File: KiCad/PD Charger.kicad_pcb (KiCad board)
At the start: 4 copper layers, 74 x 46 mm, 132 parts, among them J1 USB_C_Receptacle_USB2.0, J2 Conn_ARM_SWD_TagConnect_TC2030, J3 XT60_M, Q1 NMOS, Q2 NMOS, Q3 NMOS, Q4 NMOS, Q5 SiR5607DP, Q6 SiR5607DP, Q7 SiR5607DP, Q8 SiR5607DP, Q9 Q_Dual_NMOS_S1G1D2S2G2D1, SW1 SW_MEC_5G, SW2 SW_MEC_5G, U1 FUSB302B01MPX, U2 LMR36006BRNXT, U3 LT8390xFE, U4 STM32G431CBUx, U5 ADM1270ACPZ, U6 INA293A2, U7 TPD4E05U06DQA

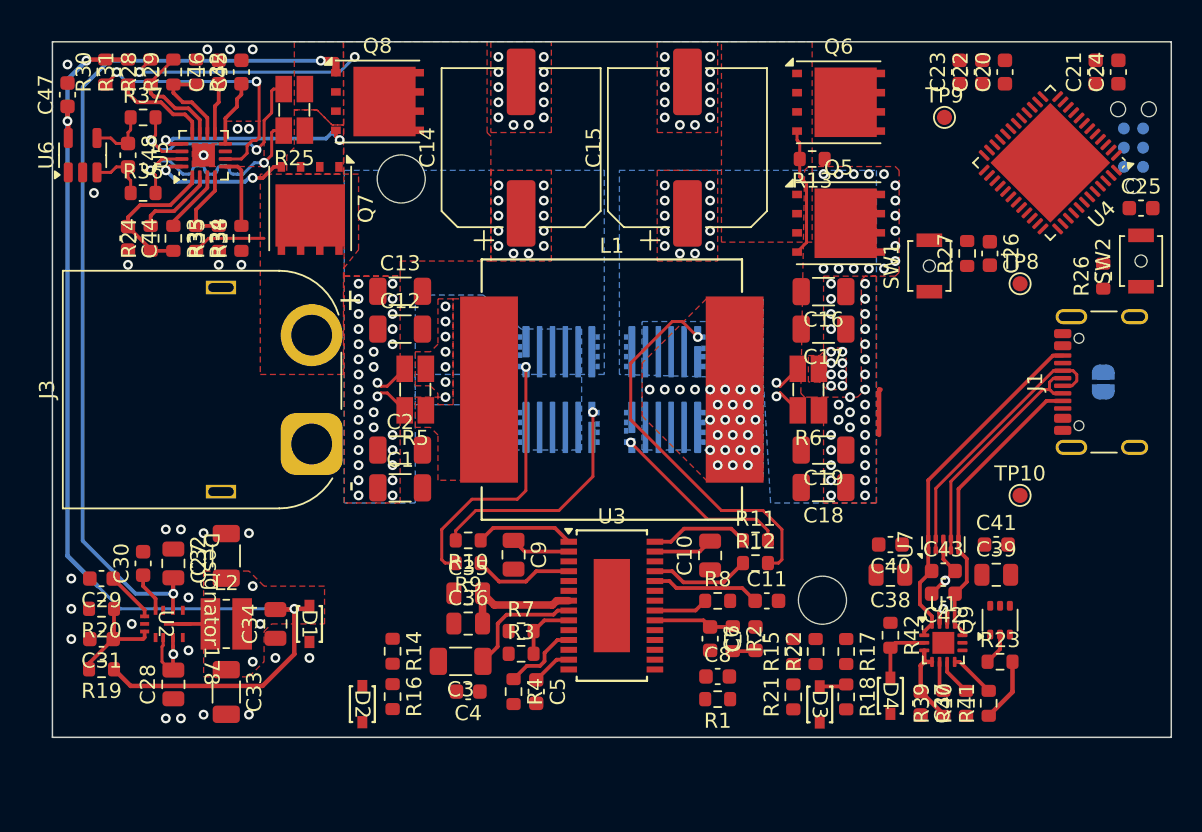
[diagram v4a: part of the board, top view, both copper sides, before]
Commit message: multi sheet redesign
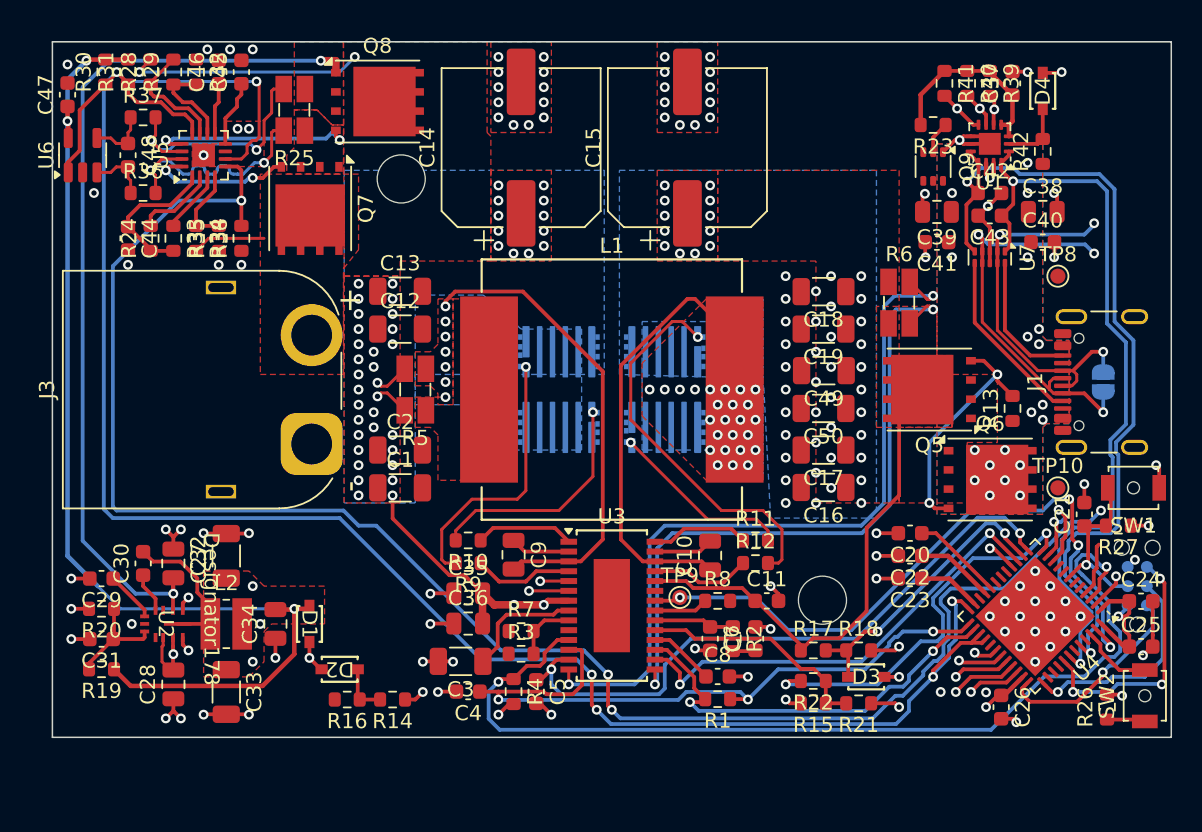
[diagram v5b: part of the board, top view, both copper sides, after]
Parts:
- added C49: 10u, Capacitor_SMD:C_1206_3216Metric, F.Cu at (63.0, 33.8)
- added C50: 10u, Capacitor_SMD:C_1206_3216Metric, F.Cu at (63.0, 36.2)
- moved C37 41.4 mm to (75.5, 14.8), turned to 90 degrees
- moved D4 41.2 mm to (77.5, 15.2), turned to 90 degrees
- moved R39 41.1 mm to (74.0, 14.8), turned to -90 degrees
- moved R41 41.1 mm to (71.0, 14.8), turned to -90 degrees
- moved R40 41.0 mm to (72.5, 14.8), turned to -90 degrees
- moved TP9 36.3 mm to (53.5, 48.8)
- moved R23 35.8 mm to (70.2, 17.5), turned to 180 degrees
- moved C24 35.0 mm to (84.0, 49.0), turned to 0 degrees
- moved C23 33.7 mm to (68.7, 47.5), turned to 180 degrees
- moved R42 33.5 mm to (77.5, 19.2), turned to 90 degrees
- moved U1 33.1 mm to (74.0, 18.8), turned to 180 degrees
- moved C22 32.4 mm to (68.7, 46.0), turned to 180 degrees
- moved C20 31.1 mm to (68.7, 44.5), turned to 180 degrees
- moved Q9 30.3 mm to (70.2, 20.2), turned to -90 degrees
- moved U4 30.0 mm to (77.0, 50.0)
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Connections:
- C4 pad 1: /DC-DC/VREF -> /REG_ON
- R1 pad 1: /DC-DC/VREF -> /REG_ON
- R1 pad 2: /DC-DC/~{PGOOD} -> /~{PGOOD}
- R30 pad 1: /Input Protection/~{FAULT} -> /ISMON
- R31 pad 1: /Input Protection/SGOOD -> /ISMON
- R38 pad 2: /Input Protection/SOURCE_EN -> /SOURCE_EN
- U3 pad 12: /DC-DC/VREF -> /REG_ON
- U3 pad 17: /DC-DC/~{PGOOD} -> /~{PGOOD}
- U4 pad 25: /MCU/REG_ON -> /REG_ON
- U4 pad 26: /MCU/~{PGOOD} -> /~{PGOOD}
- U4 pad 27: /MCU/SGOOD -> /ISMON
- U4 pad 28: /MCU/~{FAULT} -> /ISMON
- U4 pad 4: /MCU/SOURCE_EN -> /SOURCE_EN
- U5 pad 12: /Input Protection/SGOOD -> /ISMON
- U5 pad 5: /Input Protection/SOURCE_EN -> /SOURCE_EN
- U5 pad 6: /Input Protection/~{FAULT} -> /ISMON
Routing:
- net /ISMON: track 0.00 -> 137.3 mm, vias 0 -> 6
- net /SOURCE_EN: track 0.00 -> 115.6 mm, vias 0 -> 4
- net GND: track 4.63 -> 70.2 mm, vias 48 -> 119
- net /LOADEN: track 5.05 -> 65.2 mm, vias 0 -> 2
- net /USB_DN: track 16.1 -> 69.7 mm, vias 0 -> 4
- net /SDA: track 3.04 -> 54.3 mm, vias 0 -> 2
- net /SCL: track 2.43 -> 53.5 mm, vias 0 -> 2
- net /USB_DP: track 18.2 -> 68.7 mm, vias 0 -> 4
- net /~{INT}: track 2.02 -> 51.7 mm, vias 0 -> 2
- net /DC-DC/ISP: track 1.98 -> 50.4 mm, vias 1 -> 2
- net /CC: track 19.8 -> 67.7 mm, vias 0 -> 2
- net /REG_ON: track 0.00 -> 45.7 mm, vias 0 -> 3
- net /SYNC: track 0.00 -> 44.9 mm, vias 0 -> 4
- net /DC-DC/ISN: track 1.98 -> 44.3 mm, vias 1 -> 2
- net /ICTRL: track 2.70 -> 42.7 mm, vias 0 -> 2
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- added copper zone on B.Cu, net VBUS
- added copper zone on F.Cu, net VBUS
- added copper zone on In1.Cu, net VBUS
- added copper zone on In2.Cu, net VBUS
- removed copper zone on In1.Cu, net VD

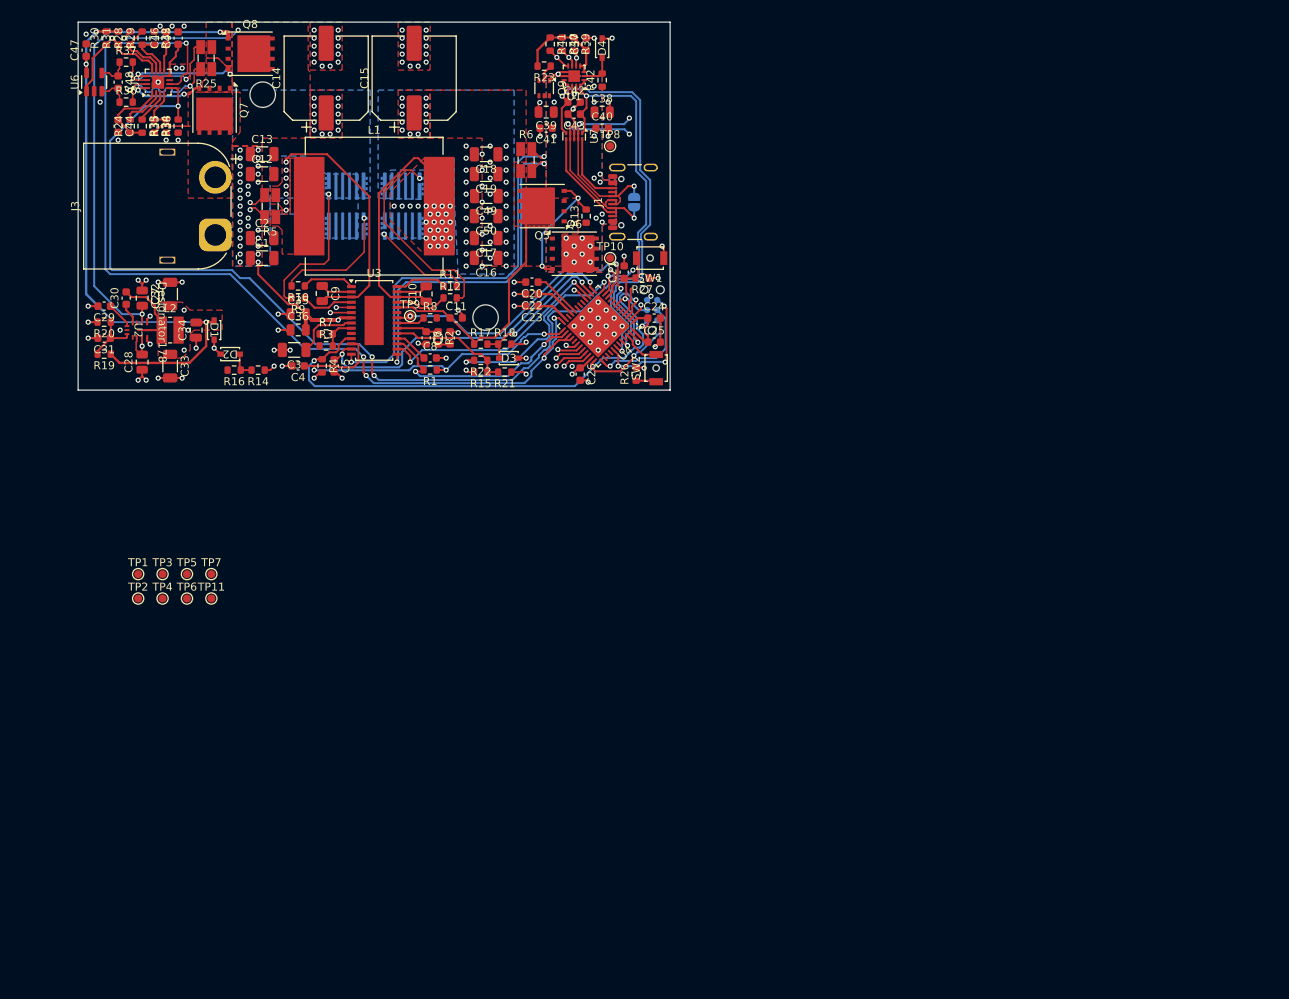
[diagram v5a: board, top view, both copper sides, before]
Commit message: standalone regulator core
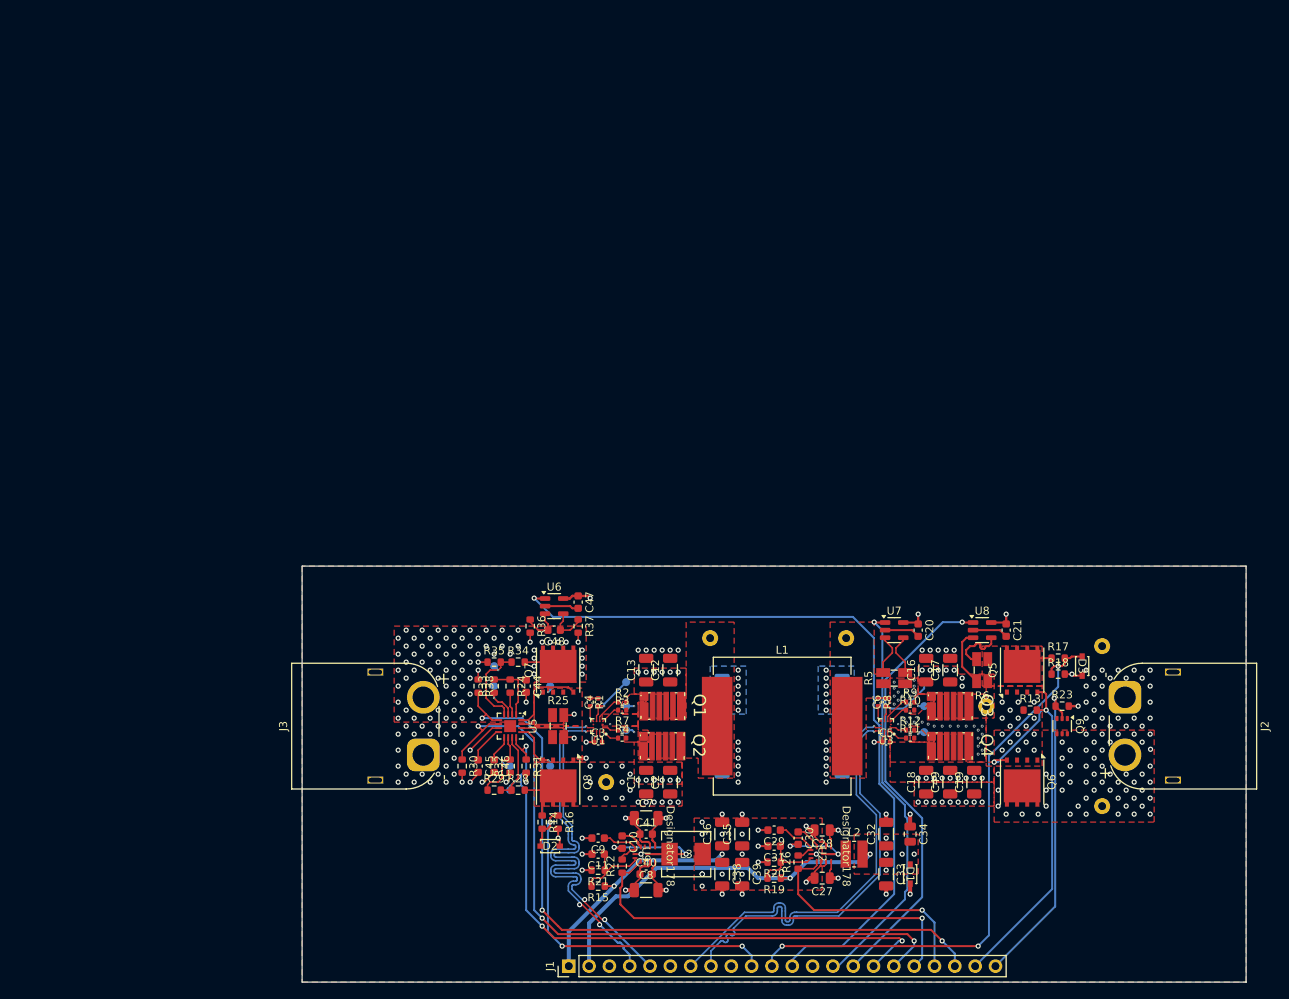
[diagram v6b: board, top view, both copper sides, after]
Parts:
- removed C22, C23, C24, C25: 0.1u, Capacitor_SMD:C_0603_1608Metric
- removed C26: 0.47u, Capacitor_SMD:C_0603_1608Metric
- removed C37: 100n, Capacitor_SMD:C_0603_1608Metric
- removed C42, C43: 330p, Capacitor_SMD:C_0603_1608Metric
- removed C50: 10u, Capacitor_SMD:C_1206_3216Metric
- removed D4: 22, Library:CR_PLZ5V1C_VIS
- removed HS1: 960-21-18-D-AB-0, Library:960-21-xx-D
- removed JP3: SolderJumper_2_Open, Jumper:SolderJumper-2_P1.3mm_Open_RoundedPad1.0x1.5mm
- removed NT6: NetTie_2, NetTie:NetTie-2_SMD_Pad0.5mm
- removed R27: 10k, Resistor_SMD:R_0603_1608Metric
- removed R39, R40, R41: 2k, Resistor_SMD:R_0603_1608Metric
- removed R42: 22k, Resistor_SMD:R_0603_1608Metric
- removed SW1, SW2: SW_MEC_5G, Button_Switch_SMD:SW_SPST_B3U-1000P-B
- removed U4: STM32G431CBUx, Package_DFN_QFN:QFN-48-1EP_7x7mm_P0.5mm_EP5.6x5.6mm
- added L3: 10u, footprints:IND_PCC-M0530M-LP_PAN, F.Cu at (88.0, 116.0)
- added TP12: TestPoint, TestPoint:TestPoint_Pad_D1.0mm, B.Cu at (64.0, 92.5)
- added TP13: TestPoint, TestPoint:TestPoint_Pad_D1.0mm, B.Cu at (66.0, 108.0)
- added TP14: TestPoint, TestPoint:TestPoint_Pad_D1.0mm, B.Cu at (66.0, 105.0)
- added TP15: TestPoint, TestPoint:TestPoint_Pad_D1.0mm, B.Cu at (71.0, 95.0)
- added TP16: TestPoint, TestPoint:TestPoint_Pad_D1.0mm, B.Cu at (71.0, 105.0)
- added TP17: TestPoint, TestPoint:TestPoint_Keystone_5000-5004_Miniature, B.Cu at (140.0, 110.0)
- added TP18: TestPoint, TestPoint:TestPoint_Keystone_5000-5004_Miniature, B.Cu at (140.0, 90.0)
- added U8: INA281A2, Package_TO_SOT_SMD:SOT-23-5, F.Cu at (125.0, 88.0)
- added U9: LMR36015BRNXT, Library:RNX0012B, F.Cu at (83.0, 116.0)
- C10: value 0.47u -> 100n; footprint Capacitor_SMD:C_0805_2012Metric -> Capacitor_SMD:C_0603_1608Metric
- C11: value 1u -> 20p
- C14, C15: moved to B.Cu
- C20, C21: value 100n -> 1uF
- C3: value 10u -> 1u; footprint Capacitor_SMD:C_1206_3216Metric -> Capacitor_SMD:C_0402_1005Metric
- C35, C36, C38, C39: value 0.47u -> 10u; footprint Capacitor_SMD:C_0805_2012Metric -> Capacitor_SMD:C_1206_3216Metric
- C4: value 0.47u -> 100n; footprint Capacitor_SMD:C_0603_1608Metric -> Capacitor_SMD:C_0402_1005Metric
- C40, C41: value 100n -> 1u
- C5: value 4.7n -> 1u; footprint Capacitor_SMD:C_0603_1608Metric -> Capacitor_SMD:C_0402_1005Metric
- C6: value 100p -> 100n; footprint Capacitor_SMD:C_0603_1608Metric -> Capacitor_SMD:C_0402_1005Metric
- C7: value 4.7n -> 10u; footprint Capacitor_SMD:C_0603_1608Metric -> Capacitor_SMD:C_1206_3216Metric
- C8: value 0.1u -> 10u; footprint Capacitor_SMD:C_0603_1608Metric -> Capacitor_SMD:C_1206_3216Metric
- C9: value 0.47u -> 1u; footprint Capacitor_SMD:C_0805_2012Metric -> Capacitor_SMD:C_0603_1608Metric
- J1: value USB_C_Receptacle_USB2.0 -> Conn_01x22; footprint Connector_USB:USB_C_Receptacle_GCT_USB4105-xx-A_16P_TopMnt_Horizontal -> Connector_PinHeader_2.54mm:PinHeader_1x22_P2.54mm_Vertical
- J2: value Conn_ARM_SWD_TagConnect_TC2030 -> Conn_01x02; footprint Connector:Tag-Connect_TC2030-IDC-NL_2x03_P1.27mm_Vertical -> Connector_AMASS:AMASS_XT60PW-M_1x02_P7.20mm_Horizontal; moved to F.Cu
- Q1, Q2, Q3, Q4: value NMOS -> EPC2302; footprint Library:ECP2302 -> KiFootprints:D0606F_100V; moved to F.Cu
- R1: value 100k -> 0; footprint Resistor_SMD:R_0603_1608Metric -> Resistor_SMD:R_0402_1005Metric
- R10, R12: footprint Resistor_SMD:R_0603_1608Metric -> Resistor_SMD:R_0402_1005Metric
- R11, R9: value 1 -> 2.2; footprint Resistor_SMD:R_0603_1608Metric -> Resistor_SMD:R_0402_1005Metric
- R15: value 36k -> 100k
- R2: value 27k -> 2.2; footprint Resistor_SMD:R_0603_1608Metric -> Resistor_SMD:R_0402_1005Metric
- R21: value 9k -> 24.9k
- R22: value ~ -> 100k
- R26: value 10k -> 100k
- R3: value 33k -> 1; footprint Resistor_SMD:R_0603_1608Metric -> Resistor_SMD:R_0402_1005Metric
- R4: value 100k -> 2.2; footprint Resistor_SMD:R_0603_1608Metric -> Resistor_SMD:R_0402_1005Metric
- R7: value 100k -> 1; footprint Resistor_SMD:R_0603_1608Metric -> Resistor_SMD:R_0402_1005Metric
- R8: value 51k -> 0; footprint Resistor_SMD:R_0603_1608Metric -> Resistor_SMD:R_0402_1005Metric
- TP1, TP2, TP3, TP4: value TestPoint_Small -> TestPoint; footprint TestPoint:TestPoint_Pad_D1.0mm -> TestPoint:TestPoint_Keystone_5000-5004_Miniature; moved to B.Cu
- TP10, TP11, TP5, TP6, TP7, TP8, TP9: value TestPoint_Small -> TestPoint; moved to B.Cu
- U1: value FUSB302B01MPX -> ~; footprint Package_DFN_QFN:WQFN-14-1EP_2.5x2.5mm_P0.5mm_EP1.45x1.45mm -> KiFootprints:WLCSP1.6x1.6-12B
- U3: value LT8390xFE -> ~; footprint Package_SO:TSSOP-28-1EP_4.4x9.7mm_P0.65mm -> KiFootprints:WLCSP1.6x1.6-12B
- U7: value TPD4E05U06DQA -> INA281A2; footprint Package_SON:USON-10_2.5x1.0mm_P0.5mm -> Package_TO_SOT_SMD:SOT-23-5
- moved C32 112.1 mm to (113.0, 113.5)
- moved C27 111.7 mm to (105.0, 119.0), turned to 180 degrees
- moved D1 110.4 mm to (116.0, 118.5)
- moved C33 109.7 mm to (113.0, 118.5)
- moved C34 109.2 mm to (116.0, 113.5), turned to -90 degrees
- moved C30 107.8 mm to (102.0, 114.0), turned to -90 degrees
- moved L2 107.7 mm to (109.0, 116.0)
- moved U2 107.7 mm to (105.0, 116.0)
- moved R20 107.6 mm to (99.0, 117.0)
- moved TP2 106.8 mm to (125.5, 97.5), turned to 180 degrees
- moved C29 106.3 mm to (99.0, 113.0)
- moved R19 106.3 mm to (99.0, 119.0)
- moved R28 105.8 mm to (67.0, 108.0), turned to 0 degrees
- moved C31 105.1 mm to (99.0, 115.0)
- moved R31 104.3 mm to (68.0, 105.0), turned to -90 degrees
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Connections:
- C10 pad 1: /DC-DC/SW2 -> /5v Regulator/BST
- C10 pad 2: /DC-DC/BST2 -> Net-(U9-SW)
- C11 pad 1: VD -> /5v Regulator/FB
- C20 pad 1: /MCU/VREF+ -> +3V3
- C21 pad 1: /MCU/~{RST} -> +3V3
- C27 pad 2: /VS_NO_LIM -> +5V
- C28 pad 2: /VS_NO_LIM -> +5V
- C3 pad 1: /DC-DC/VDD -> +5V
- C35 pad 1: GND -> +5V
- C35 pad 2: VS -> GND
- C36 pad 1: GND -> +5V
- C36 pad 2: VS -> GND
- C38 pad 1: VBUS -> +5V
- C39 pad 1: VBUS -> +5V
- C4 pad 1: /REG_ON -> Net-(U1-BOOT)
- C4 pad 2: GND -> Net-(C4-Pad2)
- C40 pad 1: VBUS -> VCC
- C41 pad 1: VBUS -> VCC
- C5 pad 1: /ICTRL -> +5V
- C6 pad 1: /DC-DC/VC -> Net-(U3-BOOT)
- C6 pad 2: GND -> Net-(C6-Pad2)
- C7 pad 1: Net-(C7-Pad1) -> VCC
- C8 pad 1: /DC-DC/SS -> VCC
- C9 pad 1: /DC-DC/BST1 -> /5v Regulator/VCC
- C9 pad 2: /DC-DC/SW1 -> GND
- D2 pad 1: /VSMON -> /VS_MON
- D3 pad 1: /VDMON -> /VD_MON
- J2 pad 1: +3V3 -> GND
- J2 pad 2: /MCU/SWDIO -> VBUS
- L1 pad 1: /DC-DC/SW1a -> /DC-DC/SW1
- L1 pad 2: /DC-DC/SW2 -> /DC-DC/SW2a
- NT5 pad 1: /VS_NO_LIM -> VCC
- Q1 pad 1: VS -> /DC-DC/G1
- Q1 pad 2: /DC-DC/G1 -> /DC-DC/SW1
- Q1 pad 3: /DC-DC/SW1 -> VS
- Q2 pad 1: /DC-DC/SW1 -> /DC-DC/G2
- Q2 pad 2: /DC-DC/G2 -> GND
- Q2 pad 3: GND -> /DC-DC/SW1
- Q3 pad 1: /DC-DC/VOUTa -> /DC-DC/G3
- Q3 pad 2: /DC-DC/G3 -> /DC-DC/SW2
- Q3 pad 3: /DC-DC/SW2 -> /DC-DC/VOUTa
- Q4 pad 1: /DC-DC/SW2 -> /DC-DC/G4
- Q4 pad 2: /DC-DC/G4 -> GND
- Q4 pad 3: GND -> /DC-DC/SW2
- Q5 pad 4: /DC-DC/LOADTG -> /OUTPUT_EN
- Q6 pad 4: /DC-DC/LOADTG -> /OUTPUT_EN
- Q9 pad 2: /LOAD_DISCHRG -> /OUTPUT_DIS
- R1 pad 1: /REG_ON -> Net-(C4-Pad2)
- R1 pad 2: /~{PGOOD} -> /DC-DC/SW1
- R10 pad 1: /DC-DC/BG1 -> Net-(U3-UGL)
- R10 pad 2: /DC-DC/G2 -> /DC-DC/G3
- R11 pad 1: /DC-DC/BG2 -> Net-(U3-LGL)
- R12 pad 1: /DC-DC/TG2 -> Net-(U3-LGH)
- R12 pad 2: /DC-DC/G3 -> /DC-DC/G4
- R13 pad 2: /DC-DC/LOADTG -> /OUTPUT_EN
- R14 pad 2: /VSMON -> /VS_MON
- R15 pad 1: /DC-DC/FB -> +5V
- R15 pad 2: VD -> /5v Regulator/FB
- R16 pad 1: /VSMON -> /VS_MON
- R17 pad 2: /VDMON -> /VD_MON
- R18 pad 1: /VDMON -> /VD_MON
- R2 pad 1: /DC-DC/VC -> Net-(U1-UGH)
- R2 pad 2: Net-(C7-Pad1) -> /DC-DC/G1
- R21 pad 1: GND -> /5v Regulator/FB
- R21 pad 2: /DC-DC/FB -> GND
- R22 pad 1: /DC-DC/FB -> /5V_GOOD
- R22 pad 2: /VCTRL -> /5v Regulator/VCC
- R23 pad 1: /LOAD_DISCHRG -> /OUTPUT_DIS
- R26 pad 1: Net-(R26-Pad1) -> /3V3_GOOD
- R26 pad 2: GND -> /3v3 Regulator/VCC
- R3 pad 1: GND -> Net-(U1-UGL)
- R3 pad 2: /DC-DC/UVLO -> /DC-DC/G1
- R30 pad 1: /ISMON -> /IS_GOOD
- R31 pad 1: /ISMON -> /VS_GOOD
- R38 pad 2: /SOURCE_EN -> /INPUT_EN
- R4 pad 1: /LOADEN -> Net-(U1-LGL)
- R4 pad 2: GND -> /DC-DC/G2
- R5 pad 1: /DC-DC/SW1a -> /DC-DC/SW2a
- R5 pad 2: /DC-DC/LSN -> /DC-DC/LSP
- R5 pad 3: /DC-DC/LSP -> /DC-DC/LSN
- R5 pad 4: /DC-DC/SW1 -> /DC-DC/SW2
- R6 pad 2: /DC-DC/ISP -> /DC-DC/IDP
- R6 pad 3: /DC-DC/ISN -> /DC-DC/IDN
- R7 pad 1: VS -> Net-(U1-LGH)
- R7 pad 2: /DC-DC/UVLO -> /DC-DC/G2
- R8 pad 1: /DC-DC/RT -> Net-(C6-Pad2)
- R8 pad 2: GND -> /DC-DC/SW2
- R9 pad 1: /DC-DC/TG1 -> Net-(U3-UGH)
- R9 pad 2: /DC-DC/G1 -> /DC-DC/G3
- TP1 pad 1: /DC-DC/G1 -> VS
- TP10 pad 1: GND -> /DC-DC/G4
- TP11 pad 1: /DC-DC/FB -> /Input Protection/UV
- TP2 pad 1: /DC-DC/SW1 -> /DC-DC/VOUTa
- TP3 pad 1: /DC-DC/G2 -> /DC-DC/SW1
- TP5 pad 1: /DC-DC/SW2 -> Net-(U1-BOOT)
- TP6 pad 1: /DC-DC/G3 -> Net-(U3-BOOT)
- TP7 pad 1: /VCTRL -> /DC-DC/G1
- TP8 pad 1: VBUS -> /DC-DC/G3
- TP9 pad 1: /SYNC -> /DC-DC/G2
- U2 pad 10: /VS_NO_LIM -> +5V
- U2 pad 2: /VS_NO_LIM -> +5V
- U2 pad 8: unconnected-(U2-PG-Pad8) -> /3V3_GOOD
- U2 pad 9: /3v3 Regulator/EN -> +5V
- U5 pad 12: /ISMON -> /VS_GOOD
- U5 pad 5: /SOURCE_EN -> /INPUT_EN
- U5 pad 6: /ISMON -> /IS_GOOD
- U6 pad 1: /ISMON -> /IS_MON
- U7 pad 1: /VCONN -> /IL_MON
- U7 pad 2: /USB_DP -> GND
- U7 pad 3: GND -> /DC-DC/LSP
- U7 pad 4: /USB_DN -> /DC-DC/LSN
- U7 pad 5: /CC -> +3V3
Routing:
- net /ISMON: track 137.3 -> 0.00 mm, vias 6 -> 0
- net /SOURCE_EN: track 115.6 -> 0.00 mm, vias 4 -> 0
- net +3V3: track 111.2 -> 211.3 mm, vias 10 -> 13
- net /IS_MON: track 0.00 -> 95.9 mm, vias 0 -> 1
- net /INPUT_EN: track 0.00 -> 91.1 mm, vias 0 -> 3
- net /IS_GOOD: track 0.00 -> 89.9 mm, vias 0 -> 3
- net +5V: track 0.00 -> 82.9 mm, vias 0 -> 16
- net /VS_GOOD: track 0.00 -> 78.5 mm, vias 0 -> 3
- net /VD_MON: track 0.00 -> 72.2 mm, vias 0 -> 3
- net /USB_DN: track 69.7 -> 0.00 mm, vias 4 -> 0
- net /USB_DP: track 68.7 -> 0.00 mm, vias 4 -> 0
- net /CC: track 67.7 -> 0.00 mm, vias 2 -> 0
- net /LOADEN: track 65.2 -> 0.00 mm, vias 2 -> 0
- net /VS_NO_LIM: track 64.3 -> 0.00 mm, vias 3 -> 0
- net /VCONN: track 60.5 -> 0.00 mm, vias 2 -> 0
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- added copper zone on In2.Cu, net +3V3
- added copper zone on F.Cu, net +5V
- added copper zone on In2.Cu, net +5V
- added copper zone on F.Cu, net /DC-DC/G1
- added copper zone on F.Cu, net /DC-DC/G2
- added copper zone on F.Cu, net /DC-DC/G3
- added copper zone on F.Cu, net /DC-DC/G4
- added copper zone on In1.Cu, net /DC-DC/SW2
- added copper zone on In2.Cu, net /DC-DC/SW2
- added copper zone on F.Cu, net /DC-DC/SW2a
- added copper zone on In1.Cu, net /DC-DC/VOUTa
- added copper zone on In2.Cu, net /DC-DC/VOUTa
- added copper zone on In1.Cu, net /Output Switch/COM_S
- added copper zone on B.Cu, net GND
- added copper zone on In1.Cu, net VIN
- added copper zone on In1.Cu, net VS
- removed copper zone on In1.Cu, net +3V3
- removed copper zone on B.Cu, net /DC-DC/SW1
- removed copper zone on F.Cu, net /DC-DC/SW1a
- removed copper zone on B.Cu, net /DC-DC/SW2
- removed copper zone on B.Cu, net VBUS
- removed copper zone on In2.Cu, net VBUS
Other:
- board size 74 x 46 mm -> 118 x 52 mm
- board text added: "Input protection"
- board text added: "Input switch node"
- board text added: "Output protection"
- board text added: "Output switch node"

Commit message: 3d models updated
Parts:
- removed the J2 at (142.8, 96.4)
- added J3: XT60_M, Connector_AMASS:AMASS_XT60PW-M_1x02_P7.20mm_Horizontal, F.Cu at (142.8, 96.4)
- renumbered J3 to J2

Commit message: finishing touches
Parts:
- moved C47 11.0 mm to (79.0, 94.5), turned to 180 degrees
- moved U6 9.92 mm to (79.0, 91.5), turned to -90 degrees
- moved R36 8.06 mm to (76.5, 88.5), turned to 90 degrees
- moved R37 7.28 mm to (76.5, 94.5)
- moved C48 6.10 mm to (76.5, 91.5), turned to 90 degrees
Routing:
- net /IS_MON: track 95.9 -> 85.0 mm
- net +3V3: track 211.3 -> 219.6 mm
- net /Input Protection/SENSE_FILTERED+: track 5.16 -> 3.86 mm
- net /Input Protection/SENSE_FILTERED-: track 5.16 -> 3.86 mm
- net /Input Protection/SENSE-: track 21.3 -> 20.2 mm, vias 2 -> 0
- net /Input Protection/SENSE+: track 21.3 -> 20.3 mm, vias 2 -> 0
- net /DC-DC/SW2: track 4.87 -> 5.79 mm
- net /DC-DC/SW1: track 4.87 -> 5.79 mm
- net GND: track 68.6 -> 68.5 mm, vias 116 -> 117
- net VIN: vias 75 -> 76
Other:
- board size 118 x 52 mm -> 122 x 47 mm
